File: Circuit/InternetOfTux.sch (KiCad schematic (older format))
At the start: 10 parts

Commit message: Added USB/Serial Bridge, buttons and auto flash.
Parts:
- removed R?: 1K, symbol R
- removed U?: ESP-12E, symbol ESP-12E
- added C? (x2): 10uF, symbol C
- added C? (x2): 0.1uF, symbol C
- added C? (x2): 1nF, symbol C
- added D? (x2): ESD05V88D-LC, symbol TVS
- added Q? (x2): S8050, TO-92, symbol S8050
- added R? (x3): 470R(1%), symbol R
- added R? (x2): 12K(1%), symbol R
- added SW?: PRGM, symbol SW_PUSH
- added SW?: RESET, symbol SW_PUSH
- added U?: CP2102, symbol CP2102
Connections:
- net labels added: ACTIVE, CLK, CMD, CTS, DCD, DSR, DTR, EN, IO0, IO12, IO13, IO14, IO15, IO16, IO17, IO18, IO19, IO2, IO21, IO22, IO23, IO25, IO26, IO27, IO32, IO33, IO34, IO35, IO4, IO5, RI, RTS, SD0, SD1, SD2, SD3, SENSOR_VN, SENSOR_VP
- net labels removed: ESP_EN, GPIO12, GPIO13, GPIO14, GPIO16
- wire segments 54 -> 139
- no-connect marks 7 -> 3
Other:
- note added: "BUTTONS"
- note added: "SIL CP2102 USB/Serial\nAutomatic ESP32 Reboot\nfor flashing.\n"
- moved on the sheet: U?, U??

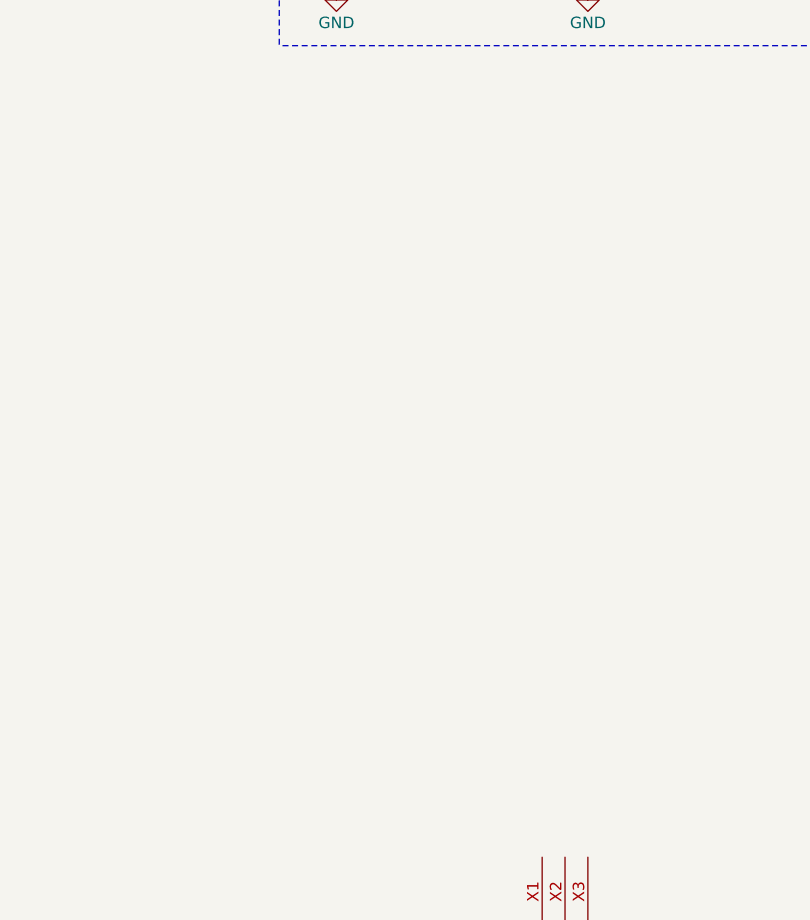
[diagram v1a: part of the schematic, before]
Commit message: Added Arduino header footprint
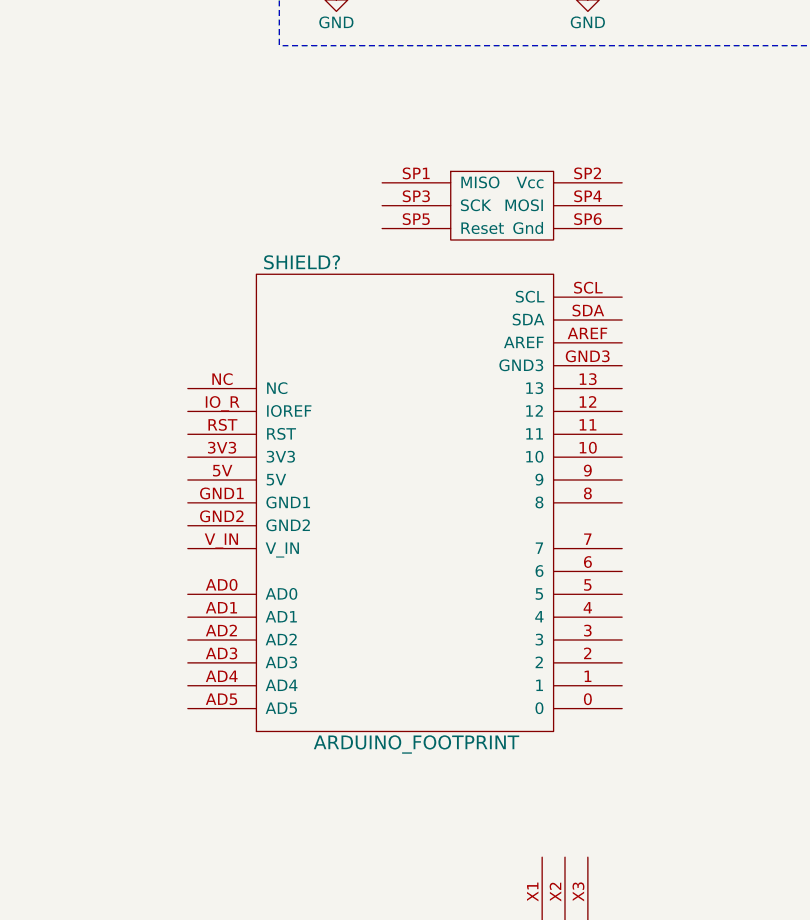
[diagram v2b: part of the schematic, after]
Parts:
- added SHIELD?: ARDUINO_FOOTPRINT, FT:ARDUINO_SHIELD, symbol ARDUINO_FOOTPRINT
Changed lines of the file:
@@
 Text Label 6000 3850 1    60   ~ 0
 IO13
+$Comp
+L ARDUINO_FOOTPRINT SHIELD?
+U 1 1 58098C9B
+P 9500 4000
+F 0 "SHIELD?" H 9050 5150 60  0000 C CNN
+F 1 "ARDUINO_FOOTPRINT" H 9550 3050 60  0000 C CNN
+F 2 "FT:ARDUINO_SHIELD" H 9500 3800 50  0001 C CNN
+F 3 "" H 9500 4000 60  0000 C CNN
+	1    9500 4000
+	1    0    0    -1
+$EndComp
 $EndSCHEMATC
